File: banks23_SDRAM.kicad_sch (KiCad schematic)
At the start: 6 parts, among them U1 NX1H35 PBGA625, U5 AS4C8M32S-6TIN

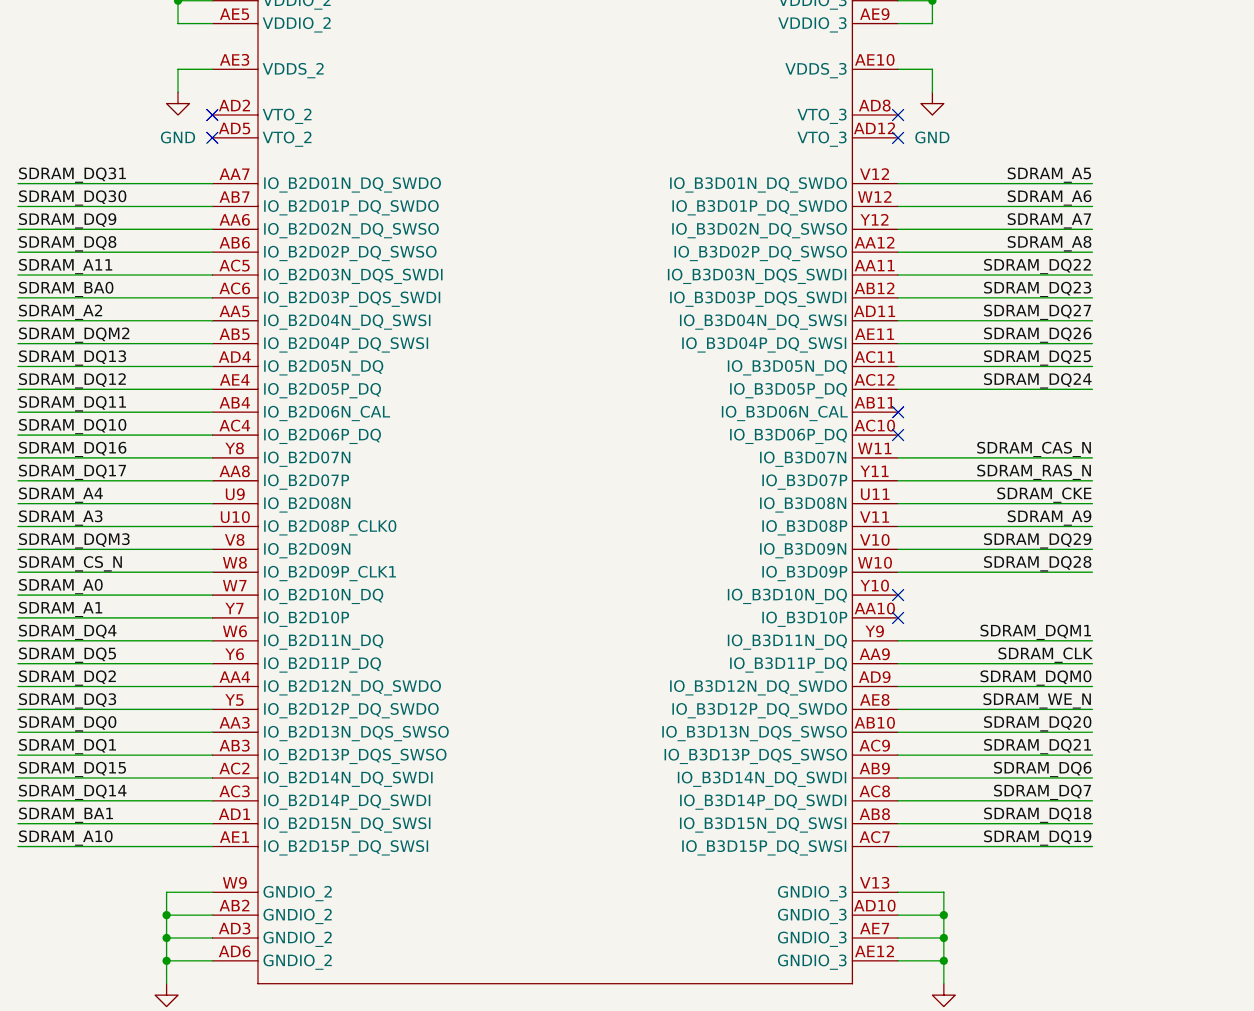
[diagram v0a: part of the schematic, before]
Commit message: SDRAM, bank5
last iteration of sdram. max optimization routing and space wise. Traced 2 frams to Bank 5. Fanout of bank 5 for DF9
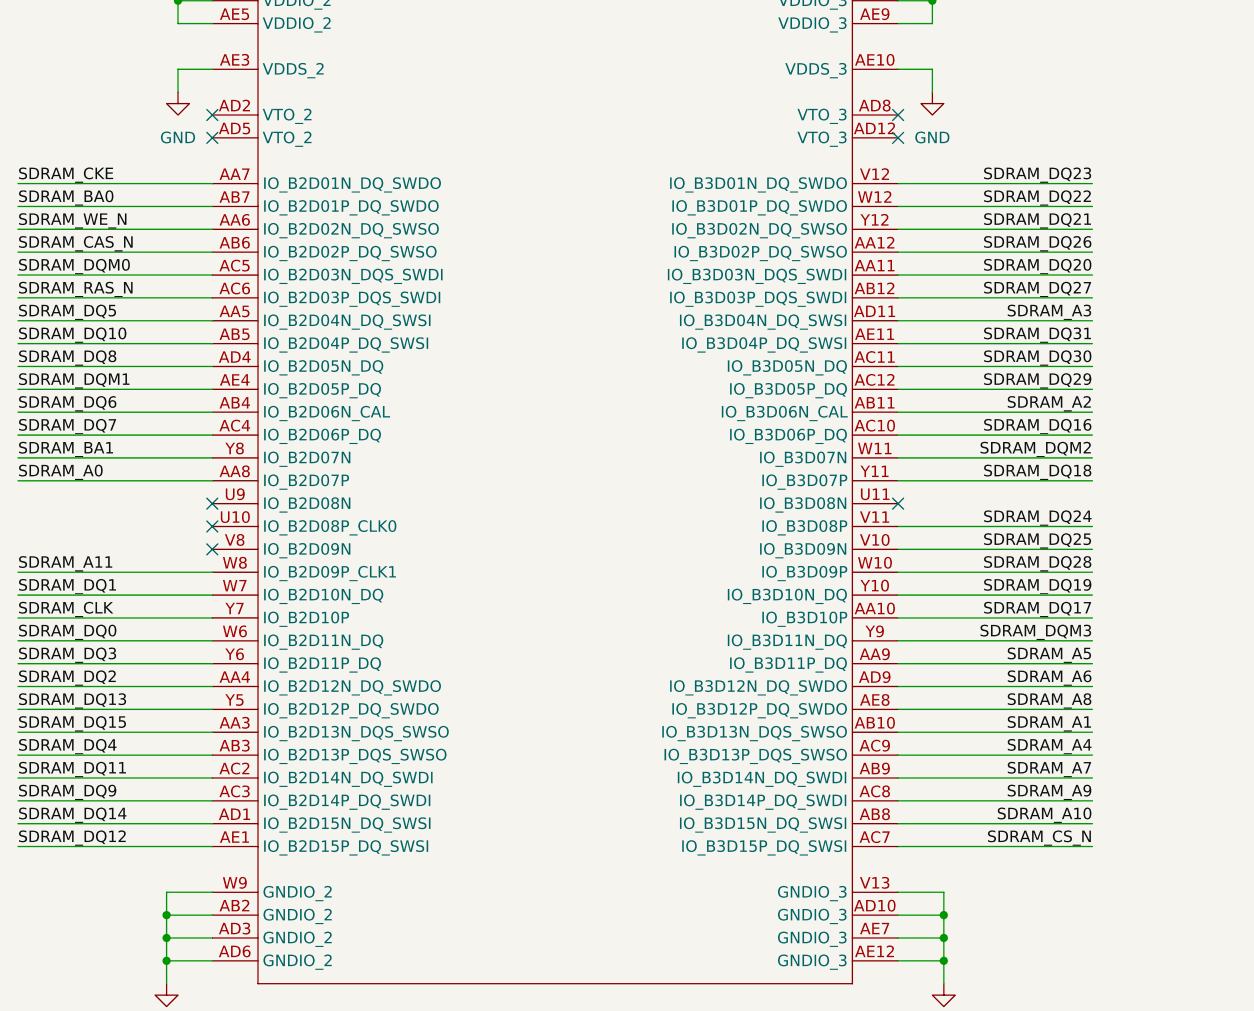
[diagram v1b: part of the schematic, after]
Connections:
- net SDRAM_A0: now also U1.AA8 (IO_B2D07P); no longer U1.W7 (IO_B2D10N_DQ)
- net SDRAM_A1: now also U1.AB10 (IO_B3D13N_DQS_SWSO); no longer U1.Y7 (IO_B2D10P)
- net SDRAM_A10: now also U1.AB8 (IO_B3D15N_DQ_SWSI); no longer U1.AE1 (IO_B2D15P_DQ_SWSI)
- net SDRAM_A11: now also U1.W8 (IO_B2D09P_CLK1); no longer U1.AC5 (IO_B2D03N_DQS_SWDI)
- net SDRAM_A2: now also U1.AB11 (IO_B3D06N_CAL); no longer U1.AA5 (IO_B2D04N_DQ_SWSI)
- net SDRAM_A3: now also U1.AD11 (IO_B3D04N_DQ_SWSI); no longer U1.U10 (IO_B2D08P_CLK0)
- net SDRAM_A4: now also U1.AC9 (IO_B3D13P_DQS_SWSO); no longer U1.U9 (IO_B2D08N)
- net SDRAM_A5: now also U1.AA9 (IO_B3D11P_DQ); no longer U1.V12 (IO_B3D01N_DQ_SWDO)
- net SDRAM_A6: now also U1.AD9 (IO_B3D12N_DQ_SWDO); no longer U1.W12 (IO_B3D01P_DQ_SWDO)
- net SDRAM_A7: now also U1.AB9 (IO_B3D14N_DQ_SWDI); no longer U1.Y12 (IO_B3D02N_DQ_SWSO)
- net SDRAM_A8: now also U1.AE8 (IO_B3D12P_DQ_SWDO); no longer U1.AA12 (IO_B3D02P_DQ_SWSO)
- net SDRAM_A9: now also U1.AC8 (IO_B3D14P_DQ_SWDI); no longer U1.V11 (IO_B3D08P)
- net SDRAM_BA0: now also U1.AB7 (IO_B2D01P_DQ_SWDO); no longer U1.AC6 (IO_B2D03P_DQS_SWDI)
- net SDRAM_BA1: now also U1.Y8 (IO_B2D07N); no longer U1.AD1 (IO_B2D15N_DQ_SWSI)
- net SDRAM_CAS_N: now also U1.AB6 (IO_B2D02P_DQ_SWSO); no longer U1.W11 (IO_B3D07N)
- net SDRAM_CKE: now also U1.AA7 (IO_B2D01N_DQ_SWDO); no longer U1.U11 (IO_B3D08N)
- net SDRAM_CLK: now also U1.Y7 (IO_B2D10P); no longer U1.AA9 (IO_B3D11P_DQ)
- net SDRAM_CS_N: now also U1.AC7 (IO_B3D15P_DQ_SWSI); no longer U1.W8 (IO_B2D09P_CLK1)
- net SDRAM_DQ0: now also U1.W6 (IO_B2D11N_DQ); no longer U1.AA3 (IO_B2D13N_DQS_SWSO)
- net SDRAM_DQ1: now also U1.W7 (IO_B2D10N_DQ); no longer U1.AB3 (IO_B2D13P_DQS_SWSO)
- net SDRAM_DQ10: now also U1.AB5 (IO_B2D04P_DQ_SWSI); no longer U1.AC4 (IO_B2D06P_DQ)
- net SDRAM_DQ11: now also U1.AC2 (IO_B2D14N_DQ_SWDI); no longer U1.AB4 (IO_B2D06N_CAL)
- net SDRAM_DQ12: now also U1.AE1 (IO_B2D15P_DQ_SWSI); no longer U1.AE4 (IO_B2D05P_DQ)
- net SDRAM_DQ13: now also U1.Y5 (IO_B2D12P_DQ_SWDO); no longer U1.AD4 (IO_B2D05N_DQ)
- net SDRAM_DQ14: now also U1.AD1 (IO_B2D15N_DQ_SWSI); no longer U1.AC3 (IO_B2D14P_DQ_SWDI)
- net SDRAM_DQ15: now also U1.AA3 (IO_B2D13N_DQS_SWSO); no longer U1.AC2 (IO_B2D14N_DQ_SWDI)
- net SDRAM_DQ16: now also U1.AC10 (IO_B3D06P_DQ); no longer U1.Y8 (IO_B2D07N)
- net SDRAM_DQ17: now also U1.AA10 (IO_B3D10P); no longer U1.AA8 (IO_B2D07P)
- net SDRAM_DQ18: now also U1.Y11 (IO_B3D07P); no longer U1.AB8 (IO_B3D15N_DQ_SWSI)
- net SDRAM_DQ19: now also U1.Y10 (IO_B3D10N_DQ); no longer U1.AC7 (IO_B3D15P_DQ_SWSI)
- net SDRAM_DQ20: now also U1.AA11 (IO_B3D03N_DQS_SWDI); no longer U1.AB10 (IO_B3D13N_DQS_SWSO)
- net SDRAM_DQ21: now also U1.Y12 (IO_B3D02N_DQ_SWSO); no longer U1.AC9 (IO_B3D13P_DQS_SWSO)
- net SDRAM_DQ22: now also U1.W12 (IO_B3D01P_DQ_SWDO); no longer U1.AA11 (IO_B3D03N_DQS_SWDI)
- net SDRAM_DQ23: now also U1.V12 (IO_B3D01N_DQ_SWDO); no longer U1.AB12 (IO_B3D03P_DQS_SWDI)
- net SDRAM_DQ24: now also U1.V11 (IO_B3D08P); no longer U1.AC12 (IO_B3D05P_DQ)
- net SDRAM_DQ25: now also U1.V10 (IO_B3D09N); no longer U1.AC11 (IO_B3D05N_DQ)
- net SDRAM_DQ26: now also U1.AA12 (IO_B3D02P_DQ_SWSO); no longer U1.AE11 (IO_B3D04P_DQ_SWSI)
- net SDRAM_DQ27: now also U1.AB12 (IO_B3D03P_DQS_SWDI); no longer U1.AD11 (IO_B3D04N_DQ_SWSI)
- net SDRAM_DQ29: now also U1.AC12 (IO_B3D05P_DQ); no longer U1.V10 (IO_B3D09N)
- net SDRAM_DQ3: now also U1.Y6 (IO_B2D11P_DQ); no longer U1.Y5 (IO_B2D12P_DQ_SWDO)
- net SDRAM_DQ30: now also U1.AC11 (IO_B3D05N_DQ); no longer U1.AB7 (IO_B2D01P_DQ_SWDO)
- net SDRAM_DQ31: now also U1.AE11 (IO_B3D04P_DQ_SWSI); no longer U1.AA7 (IO_B2D01N_DQ_SWDO)
- net SDRAM_DQ4: now also U1.AB3 (IO_B2D13P_DQS_SWSO); no longer U1.W6 (IO_B2D11N_DQ)
- net SDRAM_DQ5: now also U1.AA5 (IO_B2D04N_DQ_SWSI); no longer U1.Y6 (IO_B2D11P_DQ)
- net SDRAM_DQ6: now also U1.AB4 (IO_B2D06N_CAL); no longer U1.AB9 (IO_B3D14N_DQ_SWDI)
- net SDRAM_DQ7: now also U1.AC4 (IO_B2D06P_DQ); no longer U1.AC8 (IO_B3D14P_DQ_SWDI)
- net SDRAM_DQ8: now also U1.AD4 (IO_B2D05N_DQ); no longer U1.AB6 (IO_B2D02P_DQ_SWSO)
- net SDRAM_DQ9: now also U1.AC3 (IO_B2D14P_DQ_SWDI); no longer U1.AA6 (IO_B2D02N_DQ_SWSO)
- net SDRAM_DQM0: now also U1.AC5 (IO_B2D03N_DQS_SWDI); no longer U1.AD9 (IO_B3D12N_DQ_SWDO)
- net SDRAM_DQM1: now also U1.AE4 (IO_B2D05P_DQ); no longer U1.Y9 (IO_B3D11N_DQ)
- net SDRAM_DQM2: now also U1.W11 (IO_B3D07N); no longer U1.AB5 (IO_B2D04P_DQ_SWSI)
- net SDRAM_DQM3: now also U1.Y9 (IO_B3D11N_DQ); no longer U1.V8 (IO_B2D09N)
- net SDRAM_RAS_N: now also U1.AC6 (IO_B2D03P_DQS_SWDI); no longer U1.Y11 (IO_B3D07P)
- net SDRAM_WE_N: now also U1.AA6 (IO_B2D02N_DQ_SWSO); no longer U1.AE8 (IO_B3D12P_DQ_SWDO)

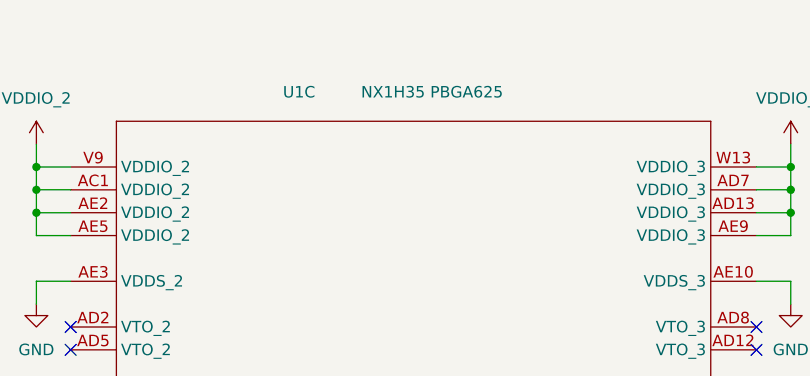
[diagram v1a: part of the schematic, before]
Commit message: finished
power planes, decoupling, ERC, DRC
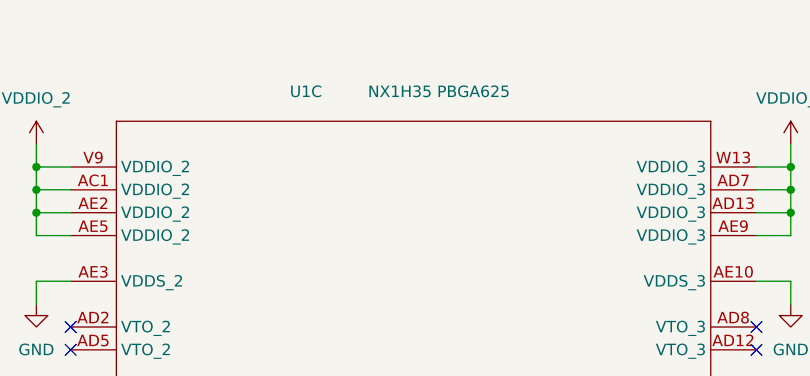
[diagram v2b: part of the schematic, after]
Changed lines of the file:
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@@
 		(dnp no)
 		(property "Reference" "U1"
-			(at 79.248 27.9908 0)
+			(at 80.01 27.94 0)
 			(effects
 				(font
@@
 		)
 		(property "Value" "NX1H35 PBGA625"
-			(at 84.328 27.9908 0)
+			(at 85.09 27.94 0)
 			(effects
 				(font
@@
 					(reference "U1")
 					(unit 3)
+				)
+				(path "/ae14ff2f-b8e3-4dd1-9329-e73906805e39/77861c37-88e9-4408-9723-ec14cfd3d63b"
+					(reference "U1")
+					(unit 3)

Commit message: pre-order adjustments
DF9 connectors footprint adjusted.
Dimensions of board edges changed.
Placement of DF9 adjusted.
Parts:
- renumbered C20 to C15, C19 to C16, C18 to C17, C16 to C18, U5 to U3
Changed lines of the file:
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@@
 		(on_board yes)
 		(dnp no)
-		(property "Reference" "C16"
+		(property "Reference" "C18"
 			(at 267.9637 30.5583 0)
 			(effects
@@
 			(project "PCB_Project"
 				(path "/ae14ff2f-b8e3-4dd1-9329-e73906805e39/3e72565b-8456-42ee-89da-a690bc2340a4"
-					(reference "C16")
+					(reference "C18")
 					(unit 1)
 				)
@@
 		(dnp no)
 		(fields_autoplaced yes)
-		(property "Reference" "#PWR034"
+		(property "Reference" "#PWR048"
 			(at 132.08 57.15 0)
 			(effects
@@
 			(project "PCB_Project"
 				(path "/ae14ff2f-b8e3-4dd1-9329-e73906805e39/3e72565b-8456-42ee-89da-a690bc2340a4"
-					(reference "#PWR034")
+					(reference "#PWR048")
 					(unit 1)
 				)
@@
 		(dnp no)
 		(fields_autoplaced yes)
-		(property "Reference" "#PWR027"
+		(property "Reference" "#PWR047"
 			(at 116.078 27.94 0)
 			(effects
@@
 			(project ""
 				(path "/ae14ff2f-b8e3-4dd1-9329-e73906805e39/3e72565b-8456-42ee-89da-a690bc2340a4"
-					(reference "#PWR027")
+					(reference "#PWR047")
 					(unit 1)
 				)
@@
 		(dnp no)
 		(fields_autoplaced yes)
-		(property "Reference" "#PWR035"
+		(property "Reference" "#PWR046"
 			(at 48.26 57.15 0)
 			(effects
@@
 			(project "PCB_Project"
 				(path "/ae14ff2f-b8e3-4dd1-9329-e73906805e39/3e72565b-8456-42ee-89da-a690bc2340a4"
-					(reference "#PWR035")
+					(reference "#PWR046")
 					(unit 1)
 				)
@@
 		(dnp no)
 		(fields_autoplaced yes)
-		(property "Reference" "#PWR09"
+		(property "Reference" "#PWR049"
 			(at 133.35 156.21 0)
 			(effects
@@
 			(project "PCB_Project"
 				(path "/ae14ff2f-b8e3-4dd1-9329-e73906805e39/3e72565b-8456-42ee-89da-a690bc2340a4"
-					(reference "#PWR09")
+					(reference "#PWR049")
 					(unit 1)
 				)
@@
 					(unit 3)
 				)
-				(path "/ae14ff2f-b8e3-4dd1-9329-e73906805e39/77861c37-88e9-4408-9723-ec14cfd3d63b"
-					(reference "U1")
-					(unit 3)
-				)
 			)
 		)
@@
 		(dnp no)
 		(fields_autoplaced yes)
-		(property "Reference" "#PWR064"
+		(property "Reference" "#PWR051"
 			(at 171.958 20.32 0)
 			(effects
@@
 			(project "PCB_Project"
 				(path "/ae14ff2f-b8e3-4dd1-9329-e73906805e39/3e72565b-8456-42ee-89da-a690bc2340a4"
-					(reference "#PWR064")
+					(reference "#PWR051")
 					(unit 1)
 				)
@@
 		(dnp no)
 		(fields_autoplaced yes)
-		(property "Reference" "#PWR063"
+		(property "Reference" "#PWR054"
 			(at 230.378 20.32 0)
 			(effects
@@
 			(project "PCB_Project"
 				(path "/ae14ff2f-b8e3-4dd1-9329-e73906805e39/3e72565b-8456-42ee-89da-a690bc2340a4"
-					(reference "#PWR063")
+					(reference "#PWR054")
 					(unit 1)
 				)
@@
 		(dnp no)
 		(fields_autoplaced yes)
-		(property "Reference" "#PWR062"
+		(property "Reference" "#PWR052"
 			(at 190.5 158.75 0)
 			(effects
@@
 			(project "PCB_Project"
 				(path "/ae14ff2f-b8e3-4dd1-9329-e73906805e39/3e72565b-8456-42ee-89da-a690bc2340a4"
-					(reference "#PWR062")
+					(reference "#PWR052")
 					(unit 1)
 				)
@@
 		(dnp no)
 		(fields_autoplaced yes)
-		(property "Reference" "#PWR061"
+		(property "Reference" "#PWR053"
 			(at 243.84 158.75 0)
 			(effects
@@
 			(project "PCB_Project"
 				(path "/ae14ff2f-b8e3-4dd1-9329-e73906805e39/3e72565b-8456-42ee-89da-a690bc2340a4"
-					(reference "#PWR061")
+					(reference "#PWR053")
 					(unit 1)
 				)
@@
 		(dnp no)
 		(fields_autoplaced yes)
-		(property "Reference" "#PWR08"
+		(property "Reference" "#PWR044"
 			(at 46.99 156.21 0)
 			(effects
@@
 			(project "PCB_Project"
 				(path "/ae14ff2f-b8e3-4dd1-9329-e73906805e39/3e72565b-8456-42ee-89da-a690bc2340a4"
-					(reference "#PWR08")
+					(reference "#PWR044")
 					(unit 1)
 				)
@@
 		(on_board yes)
 		(dnp no)
-		(property "Reference" "C20"
+		(property "Reference" "C15"
 			(at 166.3763 30.5583 0)
 			(effects
@@
 			(project "PCB_Project"
 				(path "/ae14ff2f-b8e3-4dd1-9329-e73906805e39/3e72565b-8456-42ee-89da-a690bc2340a4"
-					(reference "C20")
+					(reference "C15")
 					(unit 1)
 				)
@@
 		(on_board yes)
 		(dnp no)
-		(property "Reference" "C18"
+		(property "Reference" "C17"
 			(at 252.7363 30.48 0)
 			(effects
@@
 			(project "PCB_Project"
 				(path "/ae14ff2f-b8e3-4dd1-9329-e73906805e39/3e72565b-8456-42ee-89da-a690bc2340a4"
-					(reference "C18")
+					(reference "C17")
 					(unit 1)
 				)
@@
 		(dnp no)
 		(fields_autoplaced yes)
-		(property "Reference" "#PWR028"
+		(property "Reference" "#PWR045"
 			(at 32.258 27.94 0)
 			(effects
@@
 			(project ""
 				(path "/ae14ff2f-b8e3-4dd1-9329-e73906805e39/3e72565b-8456-42ee-89da-a690bc2340a4"
-					(reference "#PWR028")
+					(reference "#PWR045")
 					(unit 1)
 				)
@@
 		(dnp no)
 		(fields_autoplaced yes)
-		(property "Reference" "U5"
+		(property "Reference" "U3"
 			(at 217.17 33.02 0)
 			(effects
@@
 			(project "PCB_Project"
 				(path "/ae14ff2f-b8e3-4dd1-9329-e73906805e39/3e72565b-8456-42ee-89da-a690bc2340a4"
-					(reference "U5")
+					(reference "U3")
 					(unit 1)
 				)
@@
 		(on_board yes)
 		(dnp no)
-		(property "Reference" "C19"
+		(property "Reference" "C16"
 			(at 181.6037 30.48 0)
 			(effects
@@
 			(project "PCB_Project"
 				(path "/ae14ff2f-b8e3-4dd1-9329-e73906805e39/3e72565b-8456-42ee-89da-a690bc2340a4"
-					(reference "C19")
+					(reference "C16")
 					(unit 1)
 				)
@@
 		(on_board yes)
 		(dnp no)
-		(property "Reference" "#PWR066"
+		(property "Reference" "#PWR050"
 			(at 173.99 43.18 0)
 			(effects
@@
 			(project "PCB_Project"
 				(path "/ae14ff2f-b8e3-4dd1-9329-e73906805e39/3e72565b-8456-42ee-89da-a690bc2340a4"
-					(reference "#PWR066")
+					(reference "#PWR050")
 					(unit 1)
 				)
@@
 		(on_board yes)
 		(dnp no)
-		(property "Reference" "#PWR065"
+		(property "Reference" "#PWR055"
 			(at 260.35 43.18 0)
 			(effects
@@
 			(project "PCB_Project"
 				(path "/ae14ff2f-b8e3-4dd1-9329-e73906805e39/3e72565b-8456-42ee-89da-a690bc2340a4"
-					(reference "#PWR065")
+					(reference "#PWR055")
 					(unit 1)
 				)
